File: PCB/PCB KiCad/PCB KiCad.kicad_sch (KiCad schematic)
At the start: 4 parts

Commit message: Minor schematic cleanup!
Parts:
- removed H1, H2, H3, H4: MountingHole, MountingHole:MountingHole_3.2mm_M3, symbol Mechanical:MountingHole

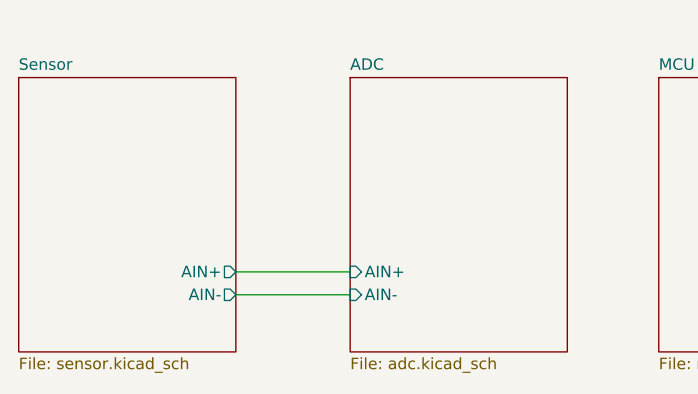
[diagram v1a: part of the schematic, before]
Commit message: Giant schematic cleanup to make more sense of the sensor circuit and just clean everything up a bit.
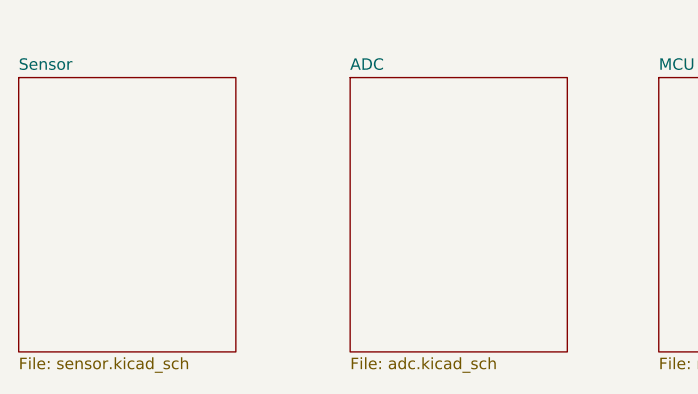
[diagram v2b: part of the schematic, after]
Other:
- sheet ADC ports: added none; removed AIN+, AIN-
- sheet Sensor ports: added none; removed AIN+, AIN-
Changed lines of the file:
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@@
 		(company "Plastic Scanner")
-	)
-	(wire
-		(pts
-			(xy 92.71 99.06) (xy 105.41 99.06)
-		)
-		(stroke
-			(width 0)
-			(type default)
-		)
-	)
-	(wire
-		(pts
-			(xy 92.71 101.6) (xy 105.41 101.6)
-		)
-		(stroke
-			(width 0)
-			(type default)
-		)
 	)
 	(sheet
@@
 			)
 		)
-		(pin "AIN-" output
-			(at 92.71 101.6 0)
-			(effects
-				(font
-					(size 1.27 1.27)
-				)
-				(justify right)
-			)
-		)
-		(pin "AIN+" output
-			(at 92.71 99.06 0)
-			(effects
-				(font
-					(size 1.27 1.27)
-				)
-				(justify right)
-			)
-		)
 		(instances
 			(project "PCB KiCad"
@@
 			)
 		)
-		(pin "AIN+" input
-			(at 105.41 99.06 180)
-			(effects
-				(font
-					(size 1.27 1.27)
-				)
-				(justify left)
-			)
-		)
-		(pin "AIN-" input
-			(at 105.41 101.6 180)
-			(effects
-				(font
-					(size 1.27 1.27)
-				)
-				(justify left)
-			)
-		)
